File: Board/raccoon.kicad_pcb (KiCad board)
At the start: 2 copper layers, 60 x 90 mm, 62 parts, among them J1 USB_B, J2 Conn_01x03, J3 Conn_01x02, J4 Conn_01x03, J5 Conn_01x02, J6 Conn_02x08_Top_Bottom, J7 Conn_01x03, J8 Conn_01x02, J9 Conn_01x06, Q1 Q_NMOS_GSD, SW1 SW_SPST, SW2 SW_SPST, U1 TJA1027T, U2 TJA1027T, U3 AMS1117-5.0, U4 AMS1117-3.3, U5 NCV7356, U6 STM32F413RGTx, U7 TJA1042T-3, U8 TJA1042T-3, U9 TJA1042T-3, Y1 16MHz

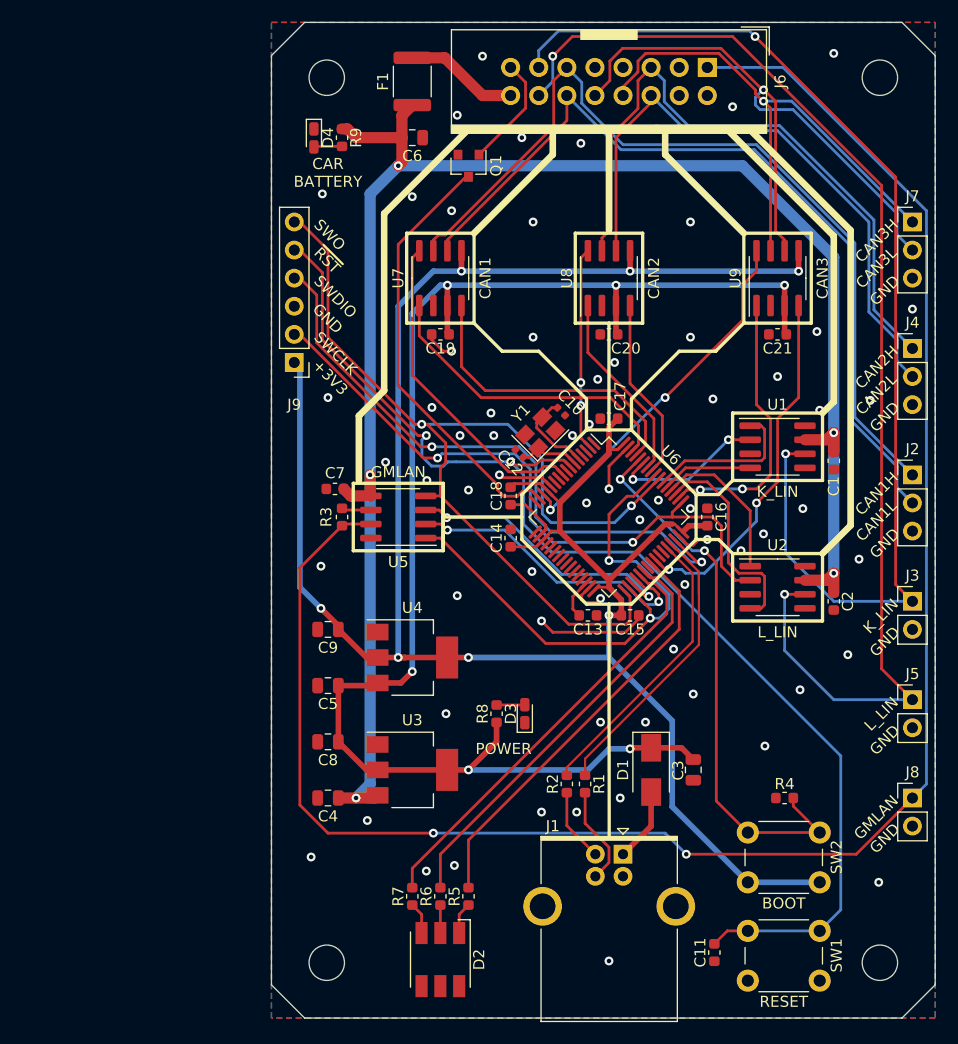
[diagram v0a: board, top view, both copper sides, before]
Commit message: deleted traces and added footprints
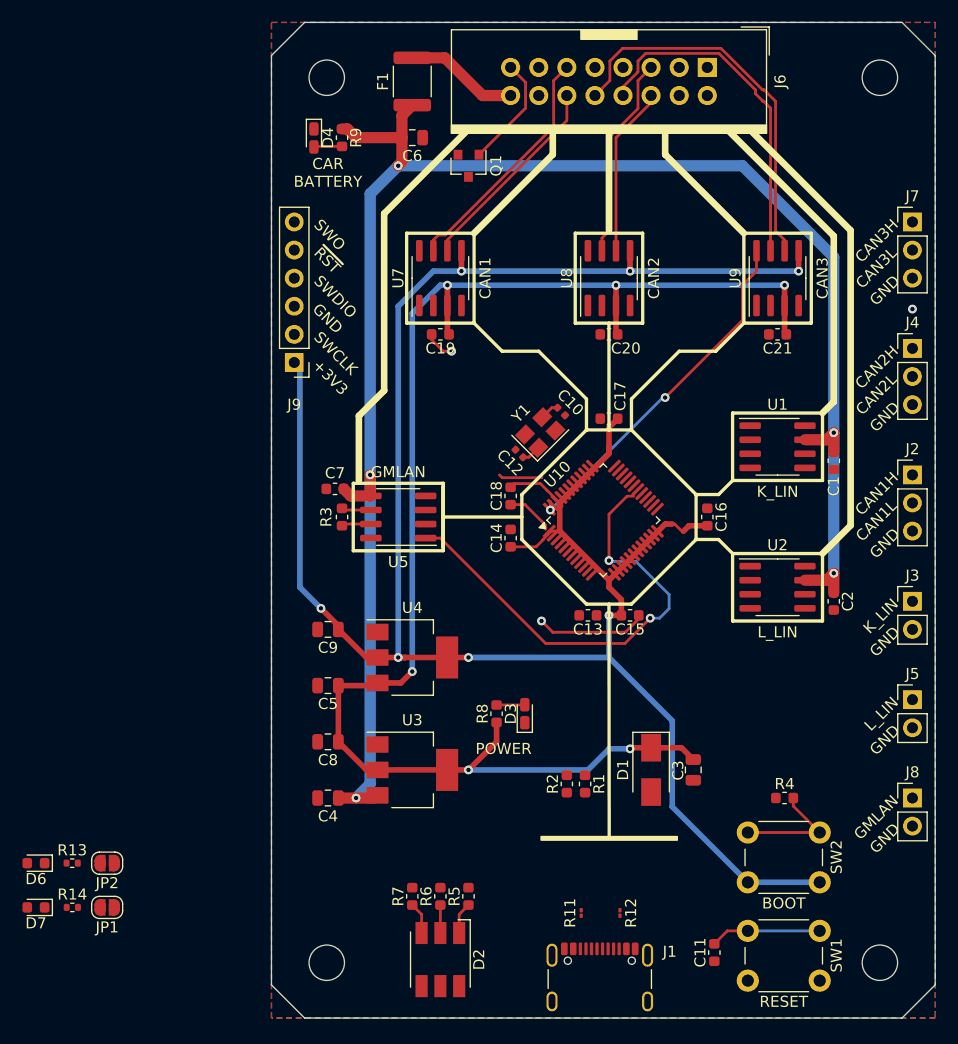
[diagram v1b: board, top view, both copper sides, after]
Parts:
- removed U6: STM32F413RGTx, Package_QFP:LQFP-64_10x10mm_P0.5mm
- added D6: D, Diode_SMD:D_0603_1608Metric, F.Cu at (91.7, 124.0)
- added D7: D, Diode_SMD:D_0603_1608Metric, F.Cu at (91.7, 128.0)
- added JP1: N/C, Jumper:SolderJumper-2_P1.3mm_Open_RoundedPad1.0x1.5mm, F.Cu at (98.2, 128.0)
- added JP2: N/C, Jumper:SolderJumper-2_P1.3mm_Open_RoundedPad1.0x1.5mm, F.Cu at (98.2, 124.0)
- added R11: 5.1k, Resistor_SMD:R_01005_0402Metric, F.Cu at (141.0, 128.5)
- added R12: 5.1k, Resistor_SMD:R_01005_0402Metric, F.Cu at (144.5, 128.5)
- added R13: 1k, Resistor_SMD:R_0402_1005Metric, F.Cu at (95.0, 124.0)
- added R14: 1k, Resistor_SMD:R_0402_1005Metric, F.Cu at (95.0, 128.0)
- added U10: STM32G473CETx, Package_QFP:LQFP-48_7x7mm_P0.5mm, F.Cu at (143.0, 93.0)
- J1: value USB_B -> USB_C_Receptacle_USB2.0_14P; footprint Connector_USB:USB_B_OST_USB-B1HSxx_Horizontal -> Connector_USB:USB_C_Receptacle_GCT_USB4105-xx-A_16P_TopMnt_Horizontal
- moved J1 12.4 mm to (142.7, 135.4), turned to 0 degrees
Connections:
- net /~RST~ renamed /~{RST}
- C13 pad 2: Net-(C13-Pad2) -> unconnected-(C13-Pad2)
- D1 pad 2: Net-(D1-Pad2) -> Net-(D1-A)
- J3 pad 1: /K_LIN -> /LIN1
- J5 pad 1: /L_LIN -> /LIN2
- J9 pad 2: /L_LIN_EN -> /SWCLK
- J9 pad 6: /GMLAN_RX -> /SWO
- R1 pad 1: /USB_DP -> /USB_DN
- R1 pad 2: Net-(J1-Pad3) -> Net-(J1-D--PadA7)
- R2 pad 1: Net-(J1-Pad2) -> Net-(J1-D+-PadA6)
- R2 pad 2: /USB_DN -> /USB_DP
- U1 pad 1: /K_LIN_RX -> /LIN1_RX
- U1 pad 2: /K_LIN_EN -> /LIN1_EN
- U1 pad 4: /K_LIN_TX -> /LIN1_TX
- U2 pad 1: /L_LIN_RX -> /LIN2_RX
- U2 pad 2: /L_LIN_EN -> /LIN2_EN
- U2 pad 4: /L_LIN_TX -> /LIN2_TX
- U7 pad 8: /~CAN1_EN~ -> /~{CAN1_EN}
- U8 pad 8: /~CAN2_EN~ -> /~{CAN2_EN}
- U9 pad 8: /~CAN3_EN~ -> /~{CAN3_EN}
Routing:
- net /GMLAN: track 167.6 -> 2.45 mm, vias 2 -> 0
- net /L_LIN: track 108.8 -> 0.00 mm, vias 2 -> 0
- net /K_LIN: track 103.7 -> 0.00 mm, vias 2 -> 0
- net /~{RST}: track 108.6 -> 10.0 mm, vias 2 -> 0
- net /GMLAN_RX: track 87.2 -> 0.00 mm, vias 2 -> 0
- net /L_LIN_EN: track 58.9 -> 0.00 mm, vias 2 -> 0
- net /CAN1L: track 76.1 -> 18.5 mm
- net /CAN1H: track 78.8 -> 21.9 mm
- net /SWDIO: track 55.6 -> 0.00 mm, vias 2 -> 0
- net /CAN2L: track 56.1 -> 14.7 mm
- net /CAN2H: track 58.4 -> 18.4 mm
- net /BOOT: track 50.6 -> 10.6 mm, vias 2 -> 0
- net Net-(Q1-D): track 39.3 -> 0.00 mm
- net /LED_BLUE: track 39.2 -> 0.00 mm
- net /LED_GREEN: track 38.7 -> 0.00 mm
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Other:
- board text added: "~{RST}"
- board text removed: "~RST~"

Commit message: uhh changed some more stuff idk
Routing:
- net /~{CAN3_EN}: track 32.1 -> 31.3 mm, vias 2 -> 1
